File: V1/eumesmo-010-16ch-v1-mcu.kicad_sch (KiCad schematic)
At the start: 17 parts, among them Q3 UMH3N, SW1 RESET, U3 TPS3820-33, U4 CH340K, U5 ESP32-WROOM-32UE-N16

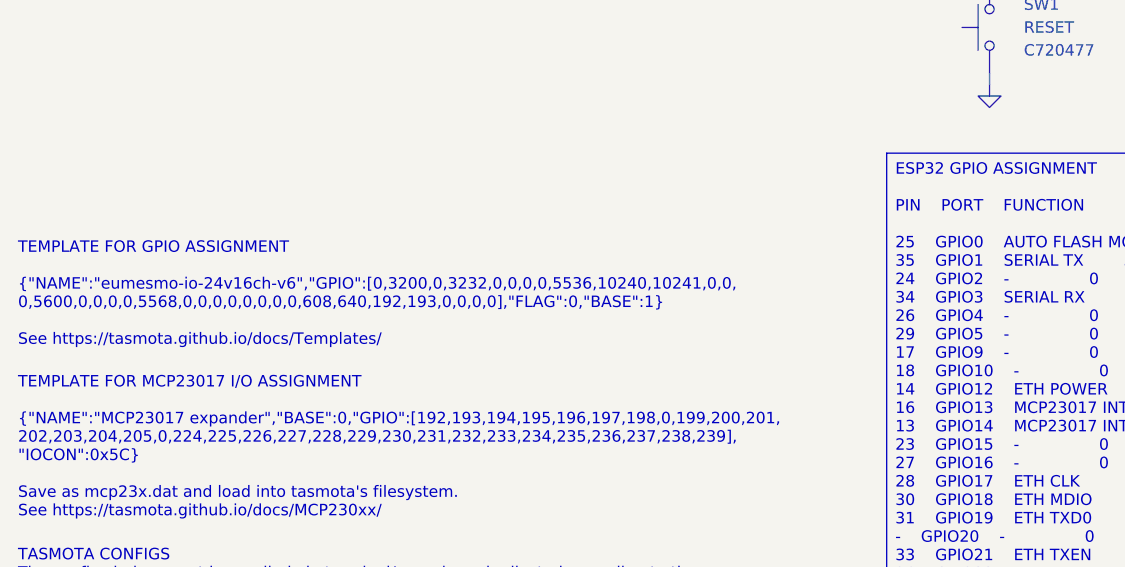
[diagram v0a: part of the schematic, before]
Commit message: Renamed all files to reflect the eumesmo branding.
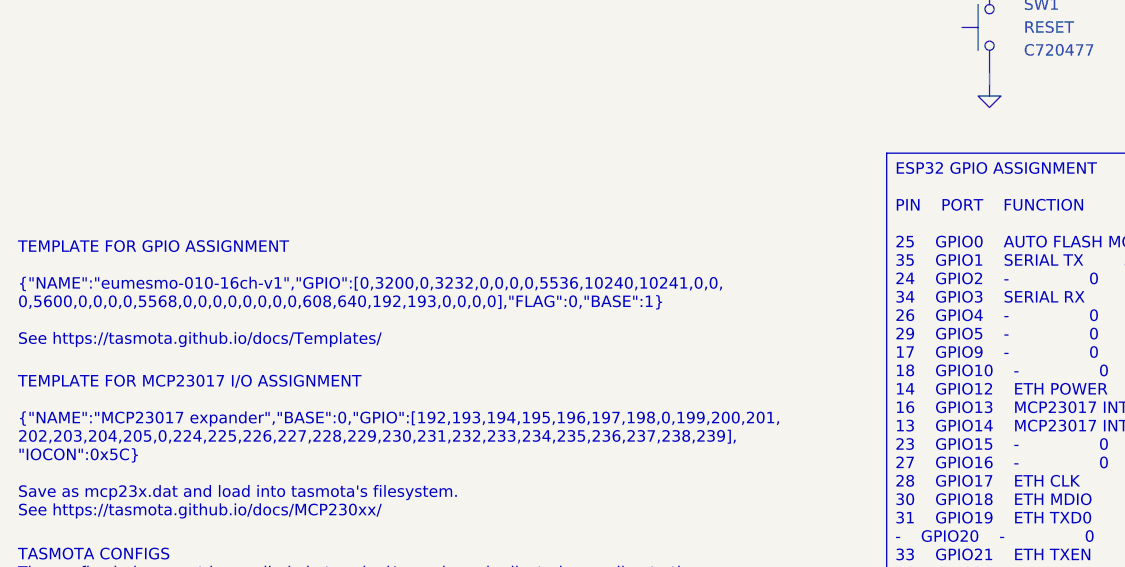
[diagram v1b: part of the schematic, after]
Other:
- note added: "TEMPLATE FOR GPIO ASSIGNMENT {"NAME":"eumesmo-010-16ch-v1","GPIO":[0,3200,0,3232,0,0,0,0,5536,10240,10241,0,0, 0,5600,0,0,0,0,5568,0,0,0,0,0,0,0,0,608,640,192,193,0,0,0,0],"FLAG":0,"BASE":1} See https://tasmota.github.io/docs/Templates/"
- note removed: "TEMPLATE FOR GPIO ASSIGNMENT {"NAME":"eumesmo-io-24v16ch-v6","GPIO":[0,3200,0,3232,0,0,0,0,5536,10240,10241,0,0, 0,5600,0,0,0,0,5568,0,0,0,0,0,0,0,0,608,640,192,193,0,0,0,0],"FLAG":0,"BASE":1} See https://tasmota.github.io/docs/Templates/"
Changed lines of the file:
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@@
 		)
 	)
-	(text "TEMPLATE FOR GPIO ASSIGNMENT\n\n{\"NAME\":\"eumesmo-io-24v16ch-v6\",\"GPIO\":[0,3200,0,3232,0,0,0,0,5536,10240,10241,0,0,\n0,5600,0,0,0,0,5568,0,0,0,0,0,0,0,0,608,640,192,193,0,0,0,0],\"FLAG\":0,\"BASE\":1}\n\nSee https://tasmota.github.io/docs/Templates/"
+	(text "TEMPLATE FOR GPIO ASSIGNMENT\n\n{\"NAME\":\"eumesmo-010-16ch-v1\",\"GPIO\":[0,3200,0,3232,0,0,0,0,5536,10240,10241,0,0,\n0,5600,0,0,0,0,5568,0,0,0,0,0,0,0,0,608,640,192,193,0,0,0,0],\"FLAG\":0,\"BASE\":1}\n\nSee https://tasmota.github.io/docs/Templates/"
 		(exclude_from_sim no)
 		(at 15.24 133.35 0)
@@
 		)
 		(instances
-			(project "eumesmo-io-24v16ch-v6"
+			(project "eumesmo-010-16ch-v1"
 				(path "/2bc5a21a-1d79-419d-a592-6852cc07b00a/f2a42251-1da5-495a-abaf-29698c5bb0fe"
 					(reference "TP11")
@@
 		)
 		(instances
-			(project "eumesmo-io-24v16ch-v6"
+			(project "eumesmo-010-16ch-v1"
 				(path "/2bc5a21a-1d79-419d-a592-6852cc07b00a/f2a42251-1da5-495a-abaf-29698c5bb0fe"
 					(reference "#PWR046")
@@
 		)
 		(instances
-			(project "eumesmo-io-24v16ch-v6"
+			(project "eumesmo-010-16ch-v1"
 				(path "/2bc5a21a-1d79-419d-a592-6852cc07b00a/f2a42251-1da5-495a-abaf-29698c5bb0fe"
 					(reference "R18")
@@
 		)
 		(instances
-			(project "eumesmo-io-24v16ch-v6"
+			(project "eumesmo-010-16ch-v1"
 				(path "/2bc5a21a-1d79-419d-a592-6852cc07b00a/f2a42251-1da5-495a-abaf-29698c5bb0fe"
 					(reference "C17")
@@
 		)
 		(instances
-			(project "eumesmo-io-24v16ch-v6"
+			(project "eumesmo-010-16ch-v1"
 				(path "/2bc5a21a-1d79-419d-a592-6852cc07b00a/f2a42251-1da5-495a-abaf-29698c5bb0fe"
 					(reference "R13")
@@
 		)
 		(instances
-			(project "eumesmo-io-24v16ch-v6"
+			(project "eumesmo-010-16ch-v1"
 				(path "/2bc5a21a-1d79-419d-a592-6852cc07b00a/f2a42251-1da5-495a-abaf-29698c5bb0fe"
 					(reference "R14")
@@
 		)
 		(instances
-			(project "eumesmo-io-24v16ch-v6"
+			(project "eumesmo-010-16ch-v1"
 				(path "/2bc5a21a-1d79-419d-a592-6852cc07b00a/f2a42251-1da5-495a-abaf-29698c5bb0fe"
 					(reference "C18")
@@
 		)
 		(instances
-			(project "eumesmo-io-24v16ch-v6"
+			(project "eumesmo-010-16ch-v1"
 				(path "/2bc5a21a-1d79-419d-a592-6852cc07b00a/f2a42251-1da5-495a-abaf-29698c5bb0fe"
 					(reference "#PWR040")
@@
 		)
 		(instances
-			(project "eumesmo-io-24v16ch-v6"
+			(project "eumesmo-010-16ch-v1"
 				(path "/2bc5a21a-1d79-419d-a592-6852cc07b00a/f2a42251-1da5-495a-abaf-29698c5bb0fe"
 					(reference "#PWR036")
@@
 		)
 		(instances
-			(project "eumesmo-io-24v16ch-v6"
+			(project "eumesmo-010-16ch-v1"
 				(path "/2bc5a21a-1d79-419d-a592-6852cc07b00a/f2a42251-1da5-495a-abaf-29698c5bb0fe"
 					(reference "TP12")
@@
 		)
 		(instances
-			(project "eumesmo-io-24v16ch-v6"
+			(project "eumesmo-010-16ch-v1"
 				(path "/2bc5a21a-1d79-419d-a592-6852cc07b00a/f2a42251-1da5-495a-abaf-29698c5bb0fe"
 					(reference "Q3")
@@
 		)
 		(instances
-			(project "eumesmo-io-24v16ch-v6"
+			(project "eumesmo-010-16ch-v1"
 				(path "/2bc5a21a-1d79-419d-a592-6852cc07b00a/f2a42251-1da5-495a-abaf-29698c5bb0fe"
 					(reference "#PWR039")
@@
 		)
 		(instances
-			(project "eumesmo-io-24v16ch-v6"
+			(project "eumesmo-010-16ch-v1"
 				(path "/2bc5a21a-1d79-419d-a592-6852cc07b00a/f2a42251-1da5-495a-abaf-29698c5bb0fe"
 					(reference "Q3")
@@
 		)
 		(instances
-			(project "eumesmo-io-24v16ch-v6"
+			(project "eumesmo-010-16ch-v1"
 				(path "/2bc5a21a-1d79-419d-a592-6852cc07b00a/f2a42251-1da5-495a-abaf-29698c5bb0fe"
 					(reference "#PWR043")
@@
 		)
 		(instances
-			(project "eumesmo-io-24v16ch-v6"
+			(project "eumesmo-010-16ch-v1"
 				(path "/2bc5a21a-1d79-419d-a592-6852cc07b00a/f2a42251-1da5-495a-abaf-29698c5bb0fe"
 					(reference "R20")
@@
 		)
 		(instances
-			(project "eumesmo-io-24v16ch-v6"
+			(project "eumesmo-010-16ch-v1"
 				(path "/2bc5a21a-1d79-419d-a592-6852cc07b00a/f2a42251-1da5-495a-abaf-29698c5bb0fe"
 					(reference "SW1")
@@
 		)
 		(instances
-			(project "eumesmo-io-24v16ch-v6"
+			(project "eumesmo-010-16ch-v1"
 				(path "/2bc5a21a-1d79-419d-a592-6852cc07b00a/f2a42251-1da5-495a-abaf-29698c5bb0fe"
 					(reference "#PWR035")
@@
 		)
 		(instances
-			(project "eumesmo-io-24v16ch-v6"
+			(project "eumesmo-010-16ch-v1"
 				(path "/2bc5a21a-1d79-419d-a592-6852cc07b00a/f2a42251-1da5-495a-abaf-29698c5bb0fe"
 					(reference "C15")
@@
 		)
 		(instances
-			(project "eumesmo-io-24v16ch-v6"
+			(project "eumesmo-010-16ch-v1"
 				(path "/2bc5a21a-1d79-419d-a592-6852cc07b00a/f2a42251-1da5-495a-abaf-29698c5bb0fe"
 					(reference "#PWR031")
@@
 		)
 		(instances
-			(project "eumesmo-io-24v16ch-v6"
+			(project "eumesmo-010-16ch-v1"
 				(path "/2bc5a21a-1d79-419d-a592-6852cc07b00a/f2a42251-1da5-495a-abaf-29698c5bb0fe"
 					(reference "#PWR032")
@@
 		)
 		(instances
-			(project "eumesmo-io-24v16ch-v6"
+			(project "eumesmo-010-16ch-v1"
 				(path "/2bc5a21a-1d79-419d-a592-6852cc07b00a/f2a42251-1da5-495a-abaf-29698c5bb0fe"
 					(reference "#PWR042")
@@
 		)
 		(instances
-			(project "eumesmo-io-24v16ch-v6"
+			(project "eumesmo-010-16ch-v1"
 				(path "/2bc5a21a-1d79-419d-a592-6852cc07b00a/f2a42251-1da5-495a-abaf-29698c5bb0fe"
 					(reference "R17")
@@
 		)
 		(instances
-			(project "eumesmo-io-24v16ch-v6"
+			(project "eumesmo-010-16ch-v1"
 				(path "/2bc5a21a-1d79-419d-a592-6852cc07b00a/f2a42251-1da5-495a-abaf-29698c5bb0fe"
 					(reference "R19")
@@
 		)
 		(instances
-			(project "eumesmo-io-24v16ch-v6"
+			(project "eumesmo-010-16ch-v1"
 				(path "/2bc5a21a-1d79-419d-a592-6852cc07b00a/f2a42251-1da5-495a-abaf-29698c5bb0fe"
 					(reference "U5")
@@
 		)
 		(instances
-			(project "eumesmo-io-24v16ch-v6"
+			(project "eumesmo-010-16ch-v1"
 				(path "/2bc5a21a-1d79-419d-a592-6852cc07b00a/f2a42251-1da5-495a-abaf-29698c5bb0fe"
 					(reference "#PWR033")
@@
 		)
 		(instances
-			(project "eumesmo-io-24v16ch-v6"
+			(project "eumesmo-010-16ch-v1"
 				(path "/2bc5a21a-1d79-419d-a592-6852cc07b00a/f2a42251-1da5-495a-abaf-29698c5bb0fe"
 					(reference "#PWR044")
@@
 		)
 		(instances
-			(project "eumesmo-io-24v16ch-v6"
+			(project "eumesmo-010-16ch-v1"
 				(path "/2bc5a21a-1d79-419d-a592-6852cc07b00a/f2a42251-1da5-495a-abaf-29698c5bb0fe"
 					(reference "U3")
@@
 		)
 		(instances
-			(project "eumesmo-io-24v16ch-v6"
+			(project "eumesmo-010-16ch-v1"
 				(path "/2bc5a21a-1d79-419d-a592-6852cc07b00a/f2a42251-1da5-495a-abaf-29698c5bb0fe"
 					(reference "#PWR041")
@@
 		)
 		(instances
-			(project "eumesmo-io-24v16ch-v6"
+			(project "eumesmo-010-16ch-v1"
 				(path "/2bc5a21a-1d79-419d-a592-6852cc07b00a/f2a42251-1da5-495a-abaf-29698c5bb0fe"
 					(reference "#PWR047")
@@
 		)
 		(instances
-			(project "eumesmo-io-24v16ch-v6"
+			(project "eumesmo-010-16ch-v1"
 				(path "/2bc5a21a-1d79-419d-a592-6852cc07b00a/f2a42251-1da5-495a-abaf-29698c5bb0fe"
 					(reference "U4")
@@
 		)
 		(instances
-			(project "eumesmo-io-24v16ch-v6"
+			(project "eumesmo-010-16ch-v1"
 				(path "/2bc5a21a-1d79-419d-a592-6852cc07b00a/f2a42251-1da5-495a-abaf-29698c5bb0fe"
 					(reference "C16")
@@
 		)
 		(instances
-			(project "eumesmo-io-24v16ch-v6"
+			(project "eumesmo-010-16ch-v1"
 				(path "/2bc5a21a-1d79-419d-a592-6852cc07b00a/f2a42251-1da5-495a-abaf-29698c5bb0fe"
 					(reference "#PWR034")
@@
 		)
 		(instances
-			(project "eumesmo-io-24v16ch-v6"
+			(project "eumesmo-010-16ch-v1"
 				(path "/2bc5a21a-1d79-419d-a592-6852cc07b00a/f2a42251-1da5-495a-abaf-29698c5bb0fe"
 					(reference "#PWR045")

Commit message: Restarting fresh
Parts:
- added R15, R16: 2k2, Tales:R_0402_1005Metric, symbol Device:R_US
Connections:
- net +3V3: now also R15.1, R16.1
- net MCPIN2INT: now reaches U5.13 (IO14)
- net MCPIN2INT: now also R16.2
- net MCPIN1INT: now reaches U5.16 (IO13)
- net MCPIN1INT: now also R15.2
- net 1WIREGPIO: now reaches U5.27 (IO16)
- no-connect marks 19 -> 16

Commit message: Development
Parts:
- removed R15, R16: 2k2, Tales:R_0402_1005Metric, symbol Device:R_US
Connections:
- net 1WIREGPIO: no longer names the net of U5.27 (IO16)
- net MCPIN1INT: no longer names the net of U5.16 (IO13)
- net MCPIN2INT: no longer names the net of U5.13 (IO14)
- no-connect marks 16 -> 19

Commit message: Development
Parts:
- U3: Technology (none) -> Voltage Monitor
- U4: Technology (none) -> USB/Serial
- U5: Technology (none) -> MCU
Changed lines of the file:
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@@
 			)
 		)
-		(property "Technology" ""
+		(property "Technology" "MCU"
 			(at 179.07 96.52 0)
 			(hide yes)
@@
 			)
 		)
+		(property "Technology" "Voltage Monitor"
+			(at 143.51 66.04 0)
+			(hide yes)
+			(show_name no)
+			(do_not_autoplace no)
+			(effects
+				(font
+					(size 1.27 1.27)
+				)
+			)
+		)
 		(pin "3"
 		)
@@
 			)
 		)
-		(property "Technology" ""
+		(property "Technology" "USB/Serial"
 			(at 63.5 72.39 0)
 			(hide yes)

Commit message: Development
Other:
- moved on the sheet: R17
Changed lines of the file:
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@@
 	)
 	(junction
-		(at 257.81 81.28)
+		(at 246.38 81.28)
 		(diameter 0)
 		(color 0 0 0 0)
@@
 	(wire
 		(pts
-			(xy 194.31 81.28) (xy 257.81 81.28)
+			(xy 194.31 81.28) (xy 246.38 81.28)
 		)
 		(stroke
@@
 	(wire
 		(pts
-			(xy 257.81 81.28) (xy 267.97 81.28)
+			(xy 246.38 81.28) (xy 267.97 81.28)
 		)
 		(stroke
@@
 	(wire
 		(pts
-			(xy 257.81 91.44) (xy 257.81 92.71)
+			(xy 246.38 91.44) (xy 246.38 92.71)
 		)
 		(stroke
@@
 	(wire
 		(pts
-			(xy 257.81 81.28) (xy 257.81 83.82)
+			(xy 246.38 81.28) (xy 246.38 83.82)
 		)
 		(stroke
@@
 	(symbol
 		(lib_id "power:GND")
-		(at 257.81 92.71 0)
+		(at 246.38 92.71 0)
 		(unit 1)
 		(body_style 1)
@@
 		(fields_autoplaced yes)
 		(property "Reference" "#PWR043"
-			(at 257.81 99.06 0)
+			(at 246.38 99.06 0)
 			(hide yes)
 			(show_name no)
@@
 		)
 		(property "Value" "GND"
-			(at 257.81 97.79 0)
+			(at 246.38 97.79 0)
 			(hide yes)
 			(show_name no)
@@
 		)
 		(property "Footprint" ""
-			(at 257.81 92.71 0)
+			(at 246.38 92.71 0)
 			(hide yes)
 			(show_name no)
@@
 		)
 		(property "Datasheet" ""
-			(at 257.81 92.71 0)
+			(at 246.38 92.71 0)
 			(hide yes)
 			(show_name no)
@@
 		)
 		(property "Description" "Power symbol creates a global label with name \"GND\" , ground"
-			(at 257.81 92.71 0)
+			(at 246.38 92.71 0)
 			(hide yes)
 			(show_name no)
@@
 	(symbol
 		(lib_id "Device:R_US")
-		(at 257.81 87.63 0)
+		(at 246.38 87.63 0)
 		(unit 1)
 		(body_style 1)
@@
 		(fields_autoplaced yes)
 		(property "Reference" "R17"
-			(at 260.35 85.0899 0)
+			(at 248.92 85.0899 0)
 			(show_name no)
 			(do_not_autoplace no)
@@
 		)
 		(property "Value" "10k"
-			(at 260.35 87.6299 0)
+			(at 248.92 87.6299 0)
 			(show_name no)
 			(do_not_autoplace no)
@@
 		)
 		(property "Footprint" "Tales:R_0402_1005Metric"
-			(at 258.826 87.884 90)
+			(at 247.396 87.884 90)
 			(hide yes)
 			(show_name no)
@@
 		)
 		(property "Datasheet" ""
-			(at 257.81 87.63 0)
+			(at 246.38 87.63 0)
 			(hide yes)
 			(show_name no)
@@
 		)
 		(property "Description" "Resistor, US symbol"
-			(at 257.81 87.63 0)
+			(at 246.38 87.63 0)
 			(hide yes)
 			(show_name no)
@@
 		)
 		(property "Mfr" "Uniroyal"
-			(at 257.81 87.63 0)
+			(at 246.38 87.63 0)
 			(hide yes)
 			(show_name no)
@@
 		)
 		(property "Vendor" "JLCPCB"
-			(at 257.81 87.63 0)
+			(at 246.38 87.63 0)
 			(hide yes)
 			(show_name no)
@@
 		)
 		(property "Mfr PN" "0402WGF1002TCE"
-			(at 257.81 87.63 0)
+			(at 246.38 87.63 0)
 			(hide yes)
 			(show_name no)
@@
 		)
 		(property "Technology" "1%"
-			(at 257.81 87.63 0)
+			(at 246.38 87.63 0)
 			(hide yes)
 			(show_name no)
@@
 		)
 		(property "Vendor PN" "C25744"
-			(at 257.81 87.63 0)
+			(at 246.38 87.63 0)
 			(hide yes)
 			(show_name no)
@@
 		)
 		(property "LCSC Part #" "C25744"
-			(at 260.35 90.1699 0)
+			(at 248.92 90.1699 0)
 			(show_name no)
 			(do_not_autoplace no)
@@
 		)
 		(property "JLCPCB BOM" "1"
-			(at 257.81 87.63 0)
+			(at 246.38 87.63 0)
 			(hide yes)
 			(show_name no)
@@
 		)
 		(property "Package" ""
-			(at 257.81 87.63 0)
+			(at 246.38 87.63 0)
 			(hide yes)
 			(show_name no)
@@
 		)
 		(property "Case" "0402/1005"
-			(at 257.81 87.63 0)
+			(at 246.38 87.63 0)
 			(hide yes)
 			(show_name no)

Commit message: Development
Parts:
- removed C15: 10uF/25V, Tales:C_0805_2012Metric, symbol Device:C_Small
